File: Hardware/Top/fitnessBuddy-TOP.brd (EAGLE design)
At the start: 38 x 38 mm, 50 parts, among them SW3 SWITCH.MOM, SW4 SWITCH.MOM, U1 NRF52832_MODULE_MDBT42, U2 FT231XS

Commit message: organized top board
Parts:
- added C17, C18: 4.7u, LinnesLab-Passives:C0603
- added C5, C6: 1u, LinnesLab-Passives:C0603
- added CHRG2: MCP73831, LinnesLab-Power:SOT23-5
- added LDO2: MIC5504, LinnesLab-Power:SOT23-5
- added R16: (no value), LinnesLab-Passives:R0603
- added R17: 100k, LinnesLab-Passives:R0603
- moved R1 2.31 mm to (1.08, 33.3), turned to 90 degrees
- moved R2 2.27 mm to (2.62, 33.3), turned to 90 degrees
- moved C14 0.58 mm to (7.73, 21.9)
- moved C1 0.23 mm to (18.2, 29.3)
- moved C2 0.23 mm to (17.8, 31.0)
- moved L1 0.23 mm to (18.2, 27.8)
- moved C4 0.23 mm to (18.3, 23.0)
- moved C3 0.23 mm to (16.9, 23.0)
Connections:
- new net N$16: CHRG2.5, R16.2
- new net N$17: C18.2, CHRG2.4, R17.2
- net 3.3V: now also C6.1, LDO2.5
- net D27/CHRG.STATUS: now also CHRG2.1, R17.1
- net GND: now also C17.2, C18.1, C5.1, C6.2, CHRG2.2, LDO2.2, R16.1
- net VIN: now also C5.2, LDO2.1, LDO2.3
- net VLIPO: now also C17.1, CHRG2.3
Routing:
- net VIN: track 1.77 -> 28.9 mm, vias 0 -> 1
- net VLIPO: track 6.20 -> 30.6 mm, vias 0 -> 1
- net D27/CHRG.STATUS: track 0.00 -> 18.5 mm, vias 0 -> 5
- net GND: track 53.7 -> 66.5 mm, vias 25 -> 27
- net 3.3V: track 0.16 -> 8.36 mm
- net SWDIO: track 5.74 -> 10.6 mm, vias 1 -> 0
- net N$17: track 0.00 -> 3.65 mm
- net N$16: track 0.00 -> 1.52 mm
- net SCL: track 24.9 -> 24.0 mm
- net A4/PPG: track 12.4 -> 13.3 mm
- net A5/TIA: track 13.4 -> 14.1 mm
- net D30/LED.CTRL: track 14.5 -> 15.1 mm
- net N$5: track 4.06 -> 4.64 mm
- net SWCLK: track 8.51 -> 8.87 mm, vias 0 -> 1

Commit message: got rid of isolated polygons
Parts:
- moved C10 1.75 mm to (1.90, 12.4)
- moved C6 0.67 mm to (9.79, 28.7)
- moved C3 0.38 mm to (16.9, 22.7)
- moved C4 0.36 mm to (18.3, 22.7)
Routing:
- net D27/CHRG.STATUS: track 18.5 -> 26.6 mm, vias 5 -> 4
- net VIN: track 28.9 -> 36.9 mm
- net GND: track 66.5 -> 69.1 mm
- net RXD.FT: track 19.4 -> 18.5 mm
- net TXD.FT: track 14.3 -> 13.4 mm

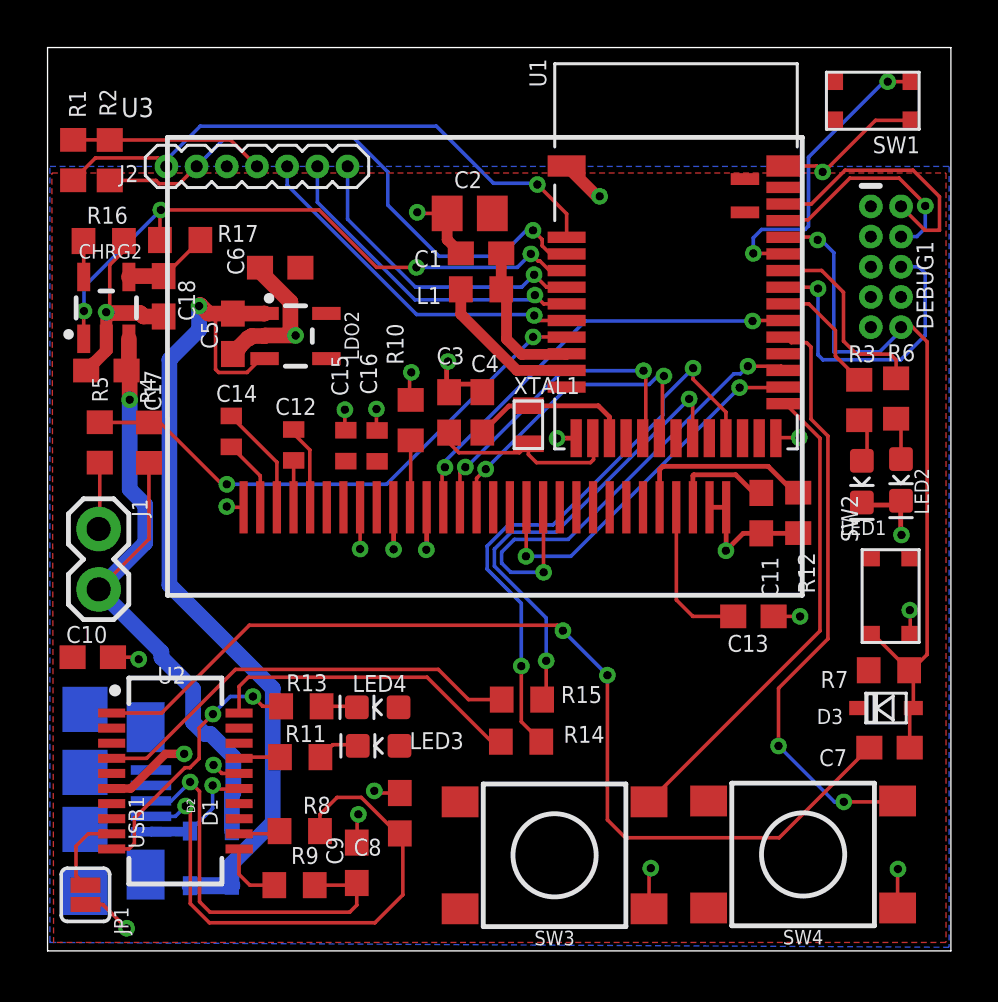
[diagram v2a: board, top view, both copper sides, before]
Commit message: reorganized bottom boards, added RTC to bottom board, and added notes to top schematic
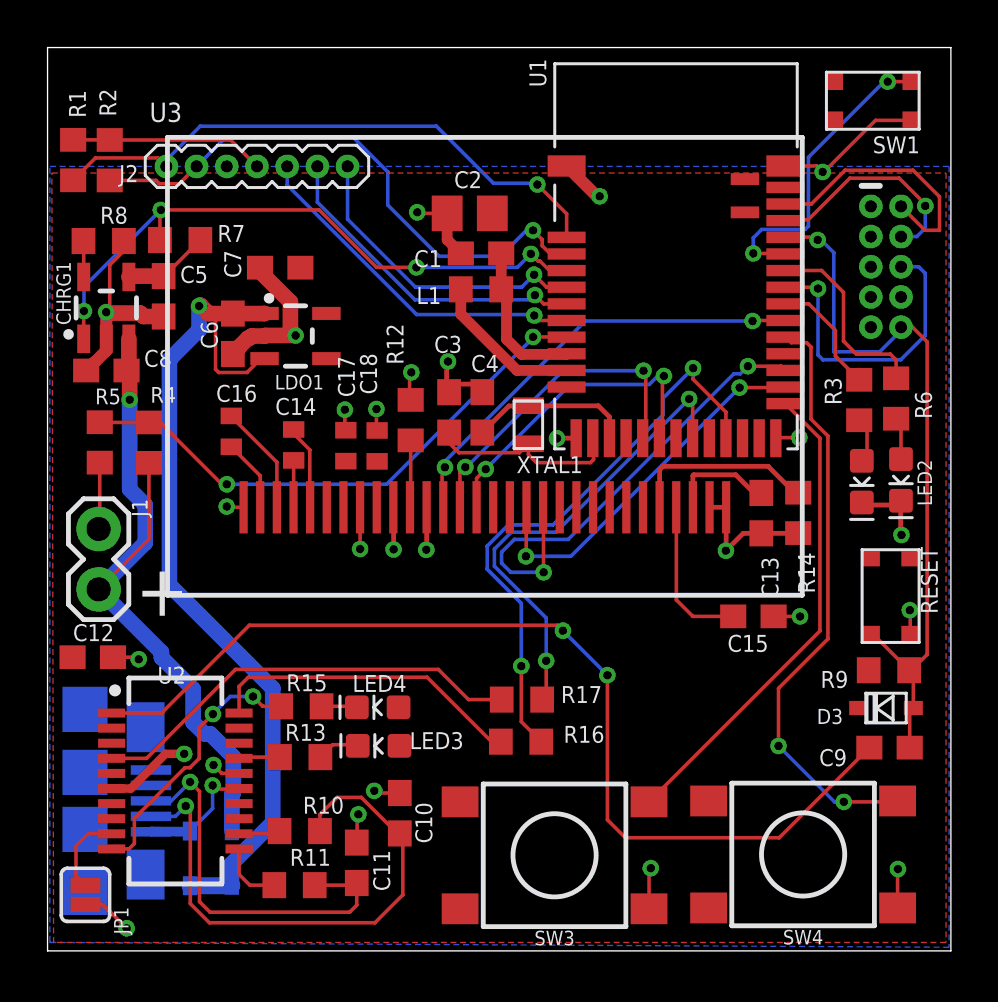
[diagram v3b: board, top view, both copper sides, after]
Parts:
- C10: value 100n -> 47p
- C11: value 10uF -> 47p
- C12: value 2.2uF -> 100n; device LinnesLab-Passives:C0402 -> LinnesLab-Passives:C0603
- C13: value 2.2uF -> 10uF
- C15: device LinnesLab-Passives:C0402 -> LinnesLab-Passives:C0603
- C17, C18: value 4.7u -> 2.2uF; device LinnesLab-Passives:C0603 -> LinnesLab-Passives:C0402
- C5: value 1u -> 4.7u
- C7: value 100n -> 1u
- C8: value 47p -> 4.7u
- C9: value 47p -> 100n
- R10: value 10k -> 27
- R11: value 1k -> 27
- R12: value 390k -> 10k
- R14: value 0 -> 390k
- R15: value 0 -> 1k
- R16: value (none) -> 0
- R17: value 100k -> 0
- R7: value 10k -> 100k
- R8: value 27 -> 5k
- R9: value 27 -> 10k
- moved R7 34.9 mm to (5.58, 29.9), turned to 0 degrees
- moved C7 32.6 mm to (9.79, 28.7), turned to 180 degrees
- moved R16 27.4 mm to (19.9, 8.80), turned to 0 degrees
- moved R9 26.6 mm to (35.4, 11.8)
- moved R8 26.2 mm to (2.36, 29.9)
- moved R17 24.1 mm to (20.0, 10.6)
- moved C9 22.9 mm to (35.4, 8.55), turned to 0 degrees
- moved C11 22.5 mm to (13.0, 3.71)
- moved C8 22.3 mm to (2.47, 24.4), turned to 180 degrees
- moved C15 18.6 mm to (29.7, 14.1), turned to 180 degrees
- moved R10 17.9 mm to (10.6, 5.04), turned to 180 degrees
- moved R12 16.8 mm to (15.3, 22.3)
- moved R14 15.1 mm to (31.6, 18.4), turned to 270 degrees
- moved C10 14.5 mm to (14.8, 5.79), turned to 270 degrees
- moved C12 12.3 mm to (1.90, 12.4), turned to 180 degrees
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- renumbered CHRG2 to CHRG1, LDO2 to LDO1, SW2 to RESET
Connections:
- net 3.3V: now also C12.2, C17.2, C18.2, C7.1, R9.2; no longer C10.2, C15.2, C16.2, C6.1, R7.2
- net D27/CHRG.STATUS: now also R7.1; no longer R17.1
- net DTR: now also C9.1; no longer C7.1
- net GND: now also C11.2, C12.1, C17.1, C6.1, C7.2, C8.2, R12.1, R14.2, R8.1; no longer C11.1, C16.1, C17.2, C6.2, C8.1, C9.2, R10.1, R12.2, R16.1
- net N$1: now also R12.2; no longer R10.2
- net N$13: now also C13.2; no longer C11.2
- net N$15: now also C15.2; no longer C13.2
- net N$16: now also R8.2; no longer R16.2
- net N$17: now also C5.2, R7.2; no longer C18.2, R17.2
- net N$2: now also R14.1; no longer R12.1
- net N$23: now also R10.2; no longer R8.2
- net N$24: now also R11.2; no longer R9.2
- net N$25: now also R13.2; no longer R11.2
- net N$26: now also R15.2; no longer R13.2
- net N$3: now also C16.2; no longer C14.2
- net N$5: now also C16.1; no longer C14.1
- net N$7: now also C14.2; no longer C12.2
- net N$8: now also C14.1; no longer C12.1
- net RESET: now also C9.2, R9.1; no longer C7.2, R7.1
- net RXD.FT: now also R17.1; no longer R15.1
- net RXD.NRF: now also R16.2; no longer R14.2
- net RXLED: now also R13.1; no longer R11.1
- net TXD.FT: now also R16.1; no longer R14.1
- net TXD.NRF: now also R17.2; no longer R15.2
- net TXLED: now also R15.1; no longer R13.1
- net USB+: now also C11.1, R11.1; no longer C9.1, R9.1
- net USB-: now also C10.2, R10.1; no longer C8.2, R8.1
- net VIN: now also C6.2; no longer C5.2
- net VLIPO: now also C8.1; no longer C17.1
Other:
- board text added: "+"
